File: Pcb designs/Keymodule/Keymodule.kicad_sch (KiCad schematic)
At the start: 105 parts, among them J1 USB connect, U1 RP2040, U2 SN74LV1T34DBV, U3 AMS1117-3.3, U4 W25Q128JVS, Y1 ABM8-272-T3

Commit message: Stared wiring ic
LED signal boost not done
But its a start
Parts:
- M_SW1, M_SW10, M_SW11, M_SW12, M_SW13, M_SW14, M_SW15, M_SW16, M_SW17, M_SW18, M_SW19, M_SW2, M_SW20, M_SW21, M_SW22, M_SW23, M_SW24, M_SW25, M_SW3, M_SW4, M_SW5, M_SW6, M_SW7, M_SW8, M_SW9: footprint 1_Custom_library:Kailh Switch 1350 -> 1_Custom_library:Kailh low profile Choc switch V1
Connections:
- net GND: no longer Y1.4 (Vdd)
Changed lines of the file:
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@@
 	)
 	(rectangle
-		(start 167.005 191.135)
-		(end 293.37 280.67)
-		(stroke
-			(width 0)
-			(type solid)
-		)
-		(fill
-			(type color)
-			(color 120 120 120 0.38)
-		)
-	)
-	(rectangle
 		(start 213.995 14.605)
 		(end 265.43 43.18)
@@
 			)
 		)
-		(property "Footprint" "1_Custom_library:Kailh Switch 1350"
+		(property "Footprint" "1_Custom_library:Kailh low profile Choc switch V1"
 			(at 280.67 231.14 0)
 			(effects
@@
 			)
 		)
-		(property "Footprint" "1_Custom_library:Kailh Switch 1350"
+		(property "Footprint" "1_Custom_library:Kailh low profile Choc switch V1"
 			(at 212.09 276.86 0)
 			(effects
@@
 			)
 		)
-		(property "Footprint" "1_Custom_library:Kailh Switch 1350"
+		(property "Footprint" "1_Custom_library:Kailh low profile Choc switch V1"
 			(at 234.95 231.14 0)
 			(effects
@@
 			)
 		)
-		(property "Footprint" "1_Custom_library:Kailh Switch 1350"
+		(property "Footprint" "1_Custom_library:Kailh low profile Choc switch V1"
 			(at 189.23 276.86 0)
 			(effects
@@
 			)
 		)
-		(property "Footprint" "1_Custom_library:Kailh Switch 1350"
+		(property "Footprint" "1_Custom_library:Kailh low profile Choc switch V1"
 			(at 234.95 276.86 0)
 			(effects
@@
 			)
 		)
-		(property "Footprint" "1_Custom_library:Kailh Switch 1350"
+		(property "Footprint" "1_Custom_library:Kailh low profile Choc switch V1"
 			(at 212.09 215.9 0)
 			(effects
@@
 			)
 		)
-		(property "Footprint" "1_Custom_library:Kailh Switch 1350"
+		(property "Footprint" "1_Custom_library:Kailh low profile Choc switch V1"
 			(at 189.23 246.38 0)
 			(effects
@@
 			)
 		)
-		(property "Footprint" "1_Custom_library:Kailh Switch 1350"
+		(property "Footprint" "1_Custom_library:Kailh low profile Choc switch V1"
 			(at 257.81 261.62 0)
 			(effects
@@
 			)
 		)
-		(property "Footprint" "1_Custom_library:Kailh Switch 1350"
+		(property "Footprint" "1_Custom_library:Kailh low profile Choc switch V1"
 			(at 257.81 231.14 0)
 			(effects
@@
 			)
 		)
-		(property "Footprint" "1_Custom_library:Kailh Switch 1350"
+		(property "Footprint" "1_Custom_library:Kailh low profile Choc switch V1"
 			(at 280.67 276.86 0)
 			(effects
@@
 			)
 		)
-		(property "Footprint" "1_Custom_library:Kailh Switch 1350"
+		(property "Footprint" "1_Custom_library:Kailh low profile Choc switch V1"
 			(at 257.81 246.38 0)
 			(effects
@@
 			)
 		)
-		(property "Footprint" "1_Custom_library:Kailh Switch 1350"
+		(property "Footprint" "1_Custom_library:Kailh low profile Choc switch V1"
 			(at 257.81 215.9 0)
 			(effects
@@
 			)
 		)
-		(property "Footprint" "1_Custom_library:Kailh Switch 1350"
+		(property "Footprint" "1_Custom_library:Kailh low profile Choc switch V1"
 			(at 189.23 215.9 0)
 			(effects
@@
 			)
 		)
-		(property "Footprint" "1_Custom_library:Kailh Switch 1350"
+		(property "Footprint" "1_Custom_library:Kailh low profile Choc switch V1"
 			(at 189.23 261.62 0)
 			(effects
@@
 			)
 		)
-		(property "Footprint" "1_Custom_library:Kailh Switch 1350"
+		(property "Footprint" "1_Custom_library:Kailh low profile Choc switch V1"
 			(at 212.09 231.14 0)
 			(effects
@@
 			)
 		)
-		(property "Footprint" "1_Custom_library:Kailh Switch 1350"
+		(property "Footprint" "1_Custom_library:Kailh low profile Choc switch V1"
 			(at 257.81 276.86 0)
 			(effects
@@
 			)
 		)
-		(property "Footprint" "1_Custom_library:Kailh Switch 1350"
+		(property "Footprint" "1_Custom_library:Kailh low profile Choc switch V1"
 			(at 234.95 246.38 0)
 			(effects
@@
 			)
 		)
-		(property "Footprint" "1_Custom_library:Kailh Switch 1350"
+		(property "Footprint" "1_Custom_library:Kailh low profile Choc switch V1"
 			(at 234.95 261.62 0)
 			(effects
@@
 	)
 	(symbol
-		(lib_id "power:GND")
-		(at 374.65 41.91 0)
-		(unit 1)
-		(exclude_from_sim no)
-		(in_bom yes)
-		(on_board yes)
-		(dnp no)
-		(fields_autoplaced yes)
-		(property "Reference" "#PWR028"
-			(at 374.65 48.26 0)
-			(effects
-				(font
-					(size 1.27 1.27)
-				)
-				(hide yes)
-			)
-		)
-		(property "Value" "GND"
-			(at 374.65 46.99 0)
-			(effects
-				(font
-					(size 1.27 1.27)
-				)
-				(hide yes)
-			)
-		)
-		(property "Footprint" ""
-			(at 374.65 41.91 0)
-			(effects
-				(font
-					(size 1.27 1.27)
-				)
-				(hide yes)
-			)
-		)
-		(property "Datasheet" ""
-			(at 374.65 41.91 0)
-			(effects
-				(font
-					(size 1.27 1.27)
-				)
-				(hide yes)
-			)
-		)
-		(property "Description" "Power symbol creates a global label with name \"GND\" , ground"
-			(at 374.65 41.91 0)
-			(effects
-				(font
-					(size 1.27 1.27)
-				)
-				(hide yes)
-			)
-		)
-		(pin "1"
-		)
-		(instances
-			(project "Keymodule"
-				(path "/8c3d34a5-d640-4303-a3a8-a4a01dc90234"
-					(reference "#PWR028")
-					(unit 1)
-				)
-			)
-		)
-	)
-	(symbol
 		(lib_id "Device:D")
 		(at 201.93 210.82 90)
@@
 			)
 		)
-		(property "Footprint" "1_Custom_library:Kailh Switch 1350"
+		(property "Footprint" "1_Custom_library:Kailh low profile Choc switch V1"
 			(at 212.09 246.38 0)
 			(effects
@@
 			)
 		)
-		(property "Footprint" "1_Custom_library:Kailh Switch 1350"
+		(property "Footprint" "1_Custom_library:Kailh low profile Choc switch V1"
 			(at 280.67 261.62 0)
 			(effects
@@
 			)
 		)
-		(property "Footprint" "1_Custom_library:Kailh Switch 1350"
+		(property "Footprint" "1_Custom_library:Kailh low profile Choc switch V1"
 			(at 280.67 246.38 0)
 			(effects
@@
 			)
 		)
-		(property "Footprint" "1_Custom_library:Kailh Switch 1350"
+		(property "Footprint" "1_Custom_library:Kailh low profile Choc switch V1"
 			(at 280.67 215.9 0)
 			(effects
@@
 			)
 		)
-		(property "Footprint" "1_Custom_library:Kailh Switch 1350"
+		(property "Footprint" "1_Custom_library:Kailh low profile Choc switch V1"
 			(at 189.23 231.14 0)
 			(effects
@@
 			)
 		)
-		(property "Footprint" "1_Custom_library:Kailh Switch 1350"
+		(property "Footprint" "1_Custom_library:Kailh low profile Choc switch V1"
 			(at 212.09 261.62 0)
 			(effects
@@
 			)
 		)
-		(property "Footprint" "1_Custom_library:Kailh Switch 1350"
+		(property "Footprint" "1_Custom_library:Kailh low profile Choc switch V1"
 			(at 234.95 215.9 0)
 			(effects

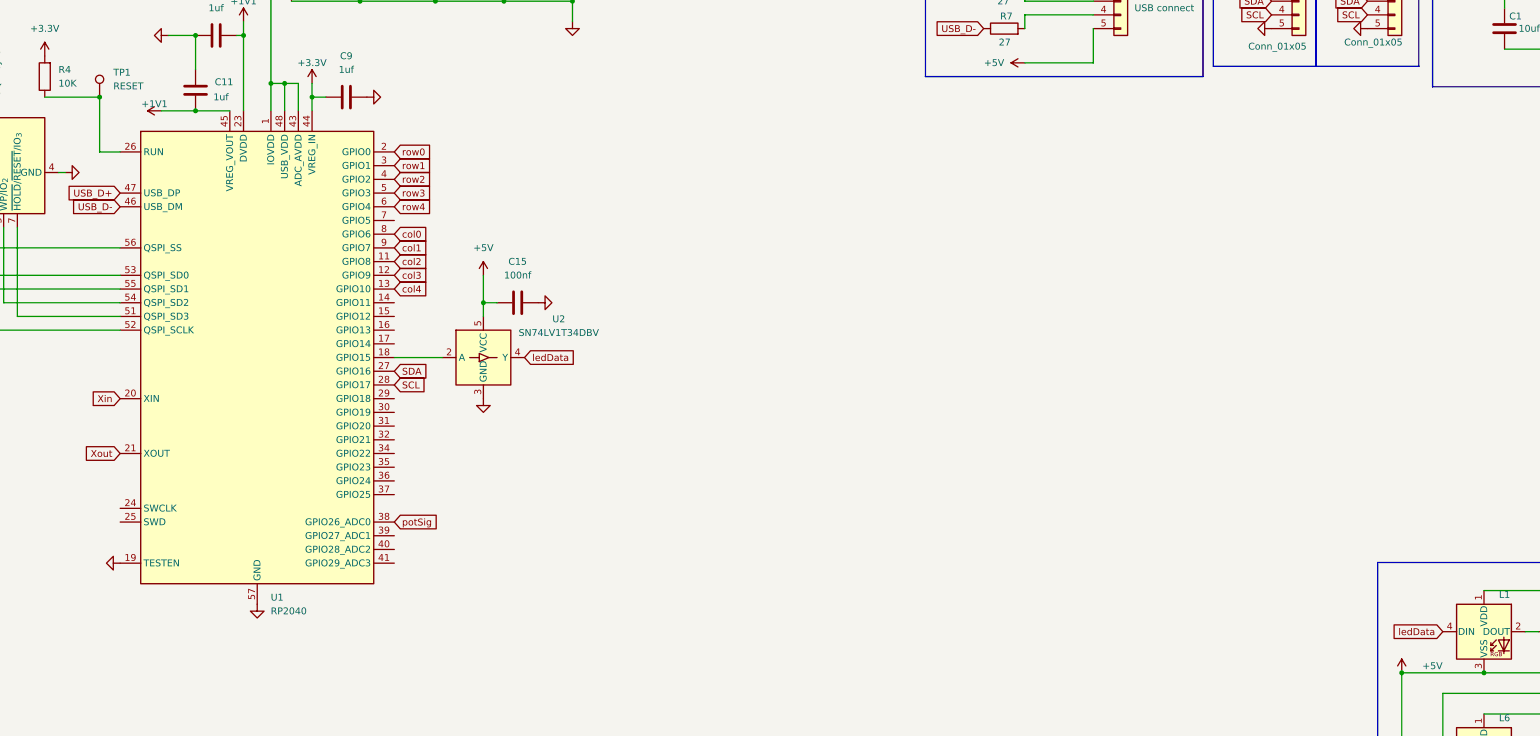
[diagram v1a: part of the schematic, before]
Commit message: Getting there (4 layers)
Made the switch to a 4 layer PCB.
het is iets duurder maar wel de moeite waard.
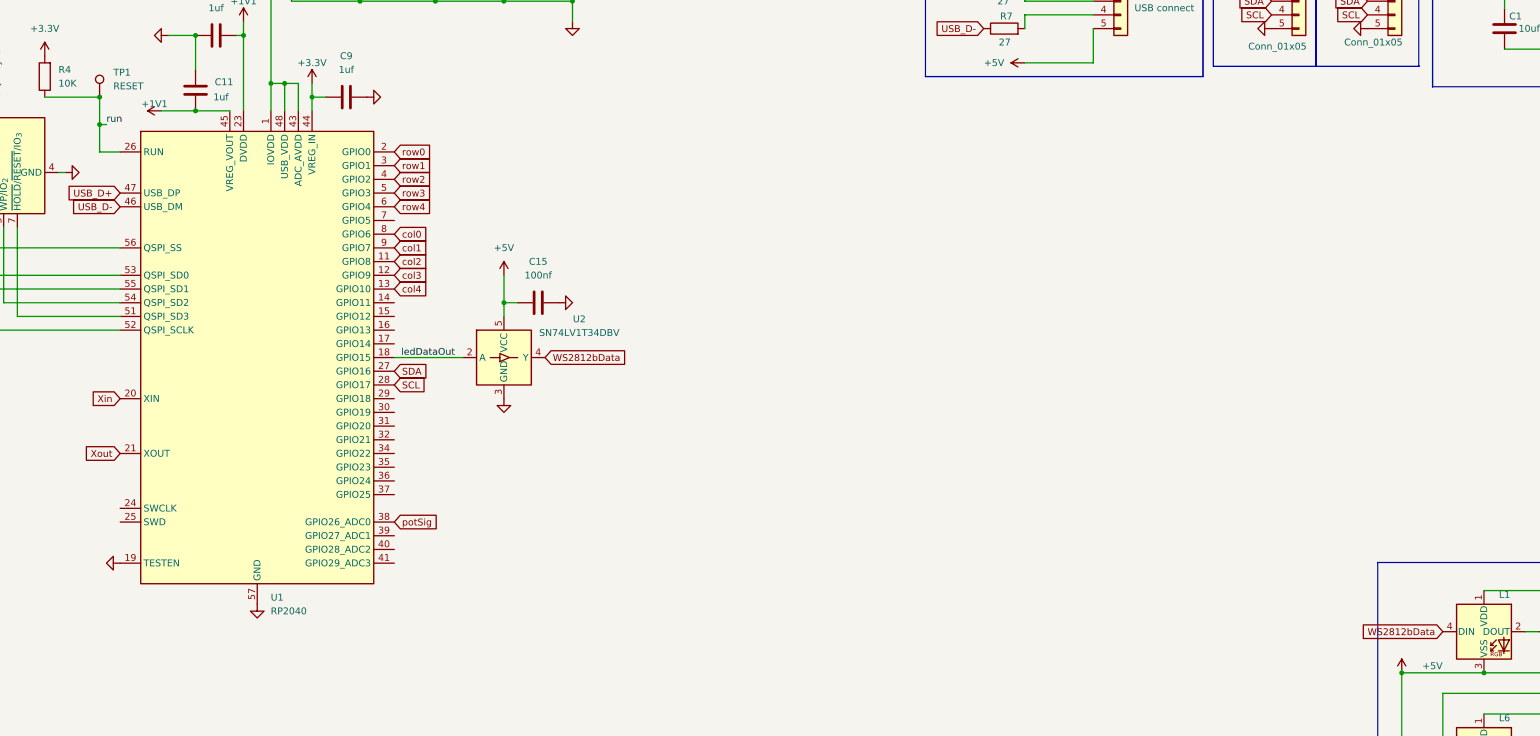
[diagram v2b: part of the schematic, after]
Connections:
- net run: now reaches R4.1, TP1.1, U1.26 (RUN)
- net ledDataOut: now reaches U1.18 (GPIO15), U2.2 (A)
- net ledData renamed WS2812bData
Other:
- moved on the sheet: C15, U2
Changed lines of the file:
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@@
 	)
 	(junction
+		(at 60.96 52.07)
+		(diameter 0)
+		(color 0 0 0 0)
+	)
+	(junction
 		(at 179.07 252.73)
 		(diameter 0)
@@
 	)
 	(junction
-		(at 132.08 85.09)
+		(at 135.89 85.09)
 		(diameter 0)
 		(color 0 0 0 0)
@@
 	(wire
 		(pts
+			(xy 62.23 52.07) (xy 60.96 52.07)
+		)
+		(stroke
+			(width 0)
+			(type default)
+		)
+	)
+	(wire
+		(pts
 			(xy 173.99 207.01) (xy 179.07 207.01)
 		)
@@
 	(wire
 		(pts
-			(xy 132.08 85.09) (xy 132.08 87.63)
+			(xy 135.89 85.09) (xy 135.89 87.63)
 		)
 		(stroke
@@
 	(wire
 		(pts
+			(xy 60.96 52.07) (xy 60.96 57.15)
+		)
+		(stroke
+			(width 0)
+			(type default)
+		)
+	)
+	(wire
+		(pts
 			(xy 40.64 71.12) (xy 40.64 82.55)
 		)
@@
 	(wire
 		(pts
-			(xy 134.62 85.09) (xy 132.08 85.09)
+			(xy 138.43 85.09) (xy 135.89 85.09)
 		)
 		(stroke
@@
 	(wire
 		(pts
-			(xy 132.08 80.01) (xy 132.08 85.09)
+			(xy 135.89 80.01) (xy 135.89 85.09)
 		)
 		(stroke
@@
 	(wire
 		(pts
-			(xy 60.96 46.99) (xy 60.96 57.15)
+			(xy 60.96 46.99) (xy 60.96 52.07)
 		)
 		(stroke
@@
 	(wire
 		(pts
-			(xy 115.57 95.25) (xy 124.46 95.25)
+			(xy 115.57 95.25) (xy 128.27 95.25)
 		)
 		(stroke
@@
 		)
 	)
+	(label "run"
+		(at 62.23 52.07 0)
+		(effects
+			(font
+				(size 1.27 1.27)
+			)
+			(justify left bottom)
+		)
+	)
+	(label "ledDataOut"
+		(at 116.84 95.25 0)
+		(effects
+			(font
+				(size 1.27 1.27)
+			)
+			(justify left bottom)
+		)
+	)
 	(global_label "row2"
 		(shape input)
@@
 		)
 	)
-	(global_label "ledData"
+	(global_label "WS2812bData"
 		(shape input)
 		(at 309.88 146.05 180)
@@
 		)
 		(property "Intersheetrefs" "${INTERSHEET_REFS}"
-			(at 300.5226 146.05 0)
+			(at 294.9281 146.05 0)
 			(effects
 				(font
@@
 		)
 	)
-	(global_label "ledData"
+	(global_label "WS2812bData"
 		(shape input)
-		(at 139.7 95.25 0)
+		(at 143.51 95.25 0)
 		(fields_autoplaced yes)
 		(effects
@@
 		)
 		(property "Intersheetrefs" "${INTERSHEET_REFS}"
-			(at 149.0574 95.25 0)
+			(at 158.4619 95.25 0)
 			(effects
 				(font
@@
 	(symbol
 		(lib_id "power:GND")
-		(at 132.08 102.87 0)
+		(at 135.89 102.87 0)
 		(unit 1)
 		(exclude_from_sim no)
@@
 		(fields_autoplaced yes)
 		(property "Reference" "#PWR027"
-			(at 132.08 109.22 0)
+			(at 135.89 109.22 0)
 			(effects
 				(font
@@
 		)
 		(property "Value" "GND"
-			(at 132.08 106.68 90)
+			(at 135.89 106.68 90)
 			(effects
 				(font
@@
 		)
 		(property "Footprint" ""
-			(at 132.08 102.87 0)
+			(at 135.89 102.87 0)
 			(effects
 				(font
@@
 		)
 		(property "Datasheet" ""
-			(at 132.08 102.87 0)
+			(at 135.89 102.87 0)
 			(effects
 				(font
@@
 		)
 		(property "Description" "Power symbol creates a global label with name \"GND\" , ground"
-			(at 132.08 102.87 0)
+			(at 135.89 102.87 0)
 			(effects
 				(font
@@
 	(symbol
 		(lib_id "Device:C")
-		(at 138.43 85.09 90)
+		(at 142.24 85.09 90)
 		(unit 1)
 		(exclude_from_sim no)
@@
 		(fields_autoplaced yes)
 		(property "Reference" "C15"
-			(at 138.43 77.47 90)
+			(at 142.24 77.47 90)
 			(effects
 				(font
@@
 		)
 		(property "Value" "100nf"
-			(at 138.43 80.01 90)
+			(at 142.24 80.01 90)
 			(effects
 				(font
@@
 		)
 		(property "Footprint" "Capacitor_SMD:C_0402_1005Metric"
-			(at 142.24 84.1248 0)
+			(at 146.05 84.1248 0)
 			(effects
 				(font
@@
 		)
 		(property "Datasheet" "~"
-			(at 138.43 85.09 0)
+			(at 142.24 85.09 0)
 			(effects
 				(font
@@
 		)
 		(property "Description" "Unpolarized capacitor"
-			(at 138.43 85.09 0)
+			(at 142.24 85.09 0)
 			(effects
 				(font
@@
 	(symbol
 		(lib_id "Logic_LevelTranslator:SN74LV1T34DBV")
-		(at 132.08 95.25 0)
+		(at 135.89 95.25 0)
 		(unit 1)
 		(exclude_from_sim no)
@@
 		(fields_autoplaced yes)
 		(property "Reference" "U2"
-			(at 146.05 88.1197 0)
+			(at 149.86 88.1197 0)
 			(effects
 				(font
@@
 		)
 		(property "Value" "SN74LV1T34DBV"
-			(at 146.05 90.6597 0)
+			(at 149.86 90.6597 0)
 			(effects
 				(font
@@
 		)
 		(property "Footprint" "Package_TO_SOT_SMD:SOT-23-5"
-			(at 148.59 101.6 0)
+			(at 152.4 101.6 0)
 			(effects
 				(font
@@
 		)
 		(property "Datasheet" "https://www.ti.com/lit/ds/symlink/sn74lv1t34.pdf"
-			(at 121.92 100.33 0)
+			(at 125.73 100.33 0)
 			(effects
 				(font
@@
 		)
 		(property "Description" "Single Power Supply, Single Buffer GATE, CMOS Logic, Level Shifter, SOT-23-5"
-			(at 132.08 95.25 0)
+			(at 135.89 95.25 0)
 			(effects
 				(font
@@
 		)
 		(property "Part number" "SN74LV1T34DBVR-TP"
-			(at 132.08 95.25 0)
+			(at 135.89 95.25 0)
 			(effects
 				(font
@@
 	(symbol
 		(lib_id "power:+5V")
-		(at 132.08 80.01 0)
+		(at 135.89 80.01 0)
 		(unit 1)
 		(exclude_from_sim no)
@@
 		(fields_autoplaced yes)
 		(property "Reference" "#PWR026"
-			(at 132.08 83.82 0)
+			(at 135.89 83.82 0)
 			(effects
 				(font
@@
 		)
 		(property "Value" "+5V"
-			(at 132.08 74.93 0)
+			(at 135.89 74.93 0)
 			(effects
 				(font
@@
 		)
 		(property "Footprint" ""
-			(at 132.08 80.01 0)
+			(at 135.89 80.01 0)
 			(effects
 				(font
@@
 		)
 		(property "Datasheet" ""
-			(at 132.08 80.01 0)
+			(at 135.89 80.01 0)
 			(effects
 				(font
@@
 		)
 		(property "Description" "Power symbol creates a global label with name \"+5V\""
-			(at 132.08 80.01 0)
+			(at 135.89 80.01 0)
 			(effects
 				(font
@@
 	(symbol
 		(lib_id "power:GND")
-		(at 142.24 85.09 90)
+		(at 146.05 85.09 90)
 		(unit 1)
 		(exclude_from_sim no)
@@
 		(fields_autoplaced yes)
 		(property "Reference" "#PWR08"
-			(at 148.59 85.09 0)
+			(at 152.4 85.09 0)
 			(effects
 				(font
@@
 		)
 		(property "Value" "GND"
-			(at 146.05 85.09 90)
+			(at 149.86 85.09 90)
 			(effects
 				(font
@@
 		)
 		(property "Footprint" ""
-			(at 142.24 85.09 0)
+			(at 146.05 85.09 0)
 			(effects
 				(font
@@
 		)
 		(property "Datasheet" ""
-			(at 142.24 85.09 0)
+			(at 146.05 85.09 0)
 			(effects
 				(font
@@
 		)
 		(property "Description" "Power symbol creates a global label with name \"GND\" , ground"
-			(at 142.24 85.09 0)
+			(at 146.05 85.09 0)
 			(effects
 				(font

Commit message: Almost done
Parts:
- removed JIn1: Conn_01x05, Connector_PinSocket_2.00mm:PinSocket_1x05_P2.00mm_Horizontal, symbol Connector_Generic:Conn_01x05
- removed JOut1: Conn_01x05, 1_Custom_library:Magnetic pogo out, symbol Connector_Generic:Conn_01x05
- added J1, J2, J4, J5: Conn_01x01, Connector_PinHeader_1.27mm:PinHeader_1x01_P1.27mm_Horizontal, symbol Connector_Generic:Conn_01x01
- added J3, J6: Conn_01x03, Connector_PinHeader_1.27mm:PinHeader_1x03_P1.27mm_Horizontal, symbol Connector_Generic:Conn_01x03
- renumbered J1 to J11
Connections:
- net +5V: now also J1.1 (Pin_1), J4.1 (Pin_1)
- net GND: now also J2.1 (Pin_1), J5.1 (Pin_1)
- net SCL: now also J3.3 (Pin_3), J6.3 (Pin_3)
- net SDA: now also J3.2 (Pin_2), J6.2 (Pin_2)
- net col0: now also U1.2 (GPIO0); no longer U1.8 (GPIO6)
- net col1: now also U1.3 (GPIO1); no longer U1.9 (GPIO7)
- net col2: now also U1.4 (GPIO2); no longer U1.11 (GPIO8)
- net col3: now also U1.5 (GPIO3); no longer U1.12 (GPIO9)
- net col4: now also U1.6 (GPIO4); no longer U1.13 (GPIO10)
- net potSig: now also J3.1 (Pin_1), J6.1 (Pin_1)
- net row0: now also U1.13 (GPIO10); no longer U1.2 (GPIO0)
- net row1: now also U1.12 (GPIO9); no longer U1.3 (GPIO1)
- net row2: now also U1.11 (GPIO8); no longer U1.4 (GPIO2)
- net row3: now also U1.9 (GPIO7); no longer U1.5 (GPIO3)
- net row4: now also U1.8 (GPIO6); no longer U1.6 (GPIO4)
